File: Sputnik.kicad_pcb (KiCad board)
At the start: 4 copper layers, 130 x 65 mm, 177 parts, among them IC1 EP4CE10F17, J1 Pinheader_2x5_TH_WALL, P1 USB_A, U1 SN74LVC2T45, U10 SN74LVC8T245, U11 SN74LVC8T245, U12 SN74LVC8T245, U13 SN74LVC8T245, U14 SN74LVC8T245, U15 SN74LVC8T245, U16 SN74LVC2T45, U17 SN74LVC2T45, U18 SN74LVC2T45, U19 SN74LVC1G07DCK, U2 SN74LVC2T45, U20 SN74LVC2T45, U21 EPCS4, U22 W9751G6KB, U23 FT313HL-LQFP64-0.5, U24 TLV62569P, U25 TPS2024D, U3 SN74LVC1G07DCK, U4 SN74LVC2T45, U5 DM9000B, U6 93LC46, U7 74LVC2G07, U8 Pulse-J00-0045NL, U9 SN74LVC8T245, X2 Zorro_Connector, Y1 25MHz, Y2 12MHz

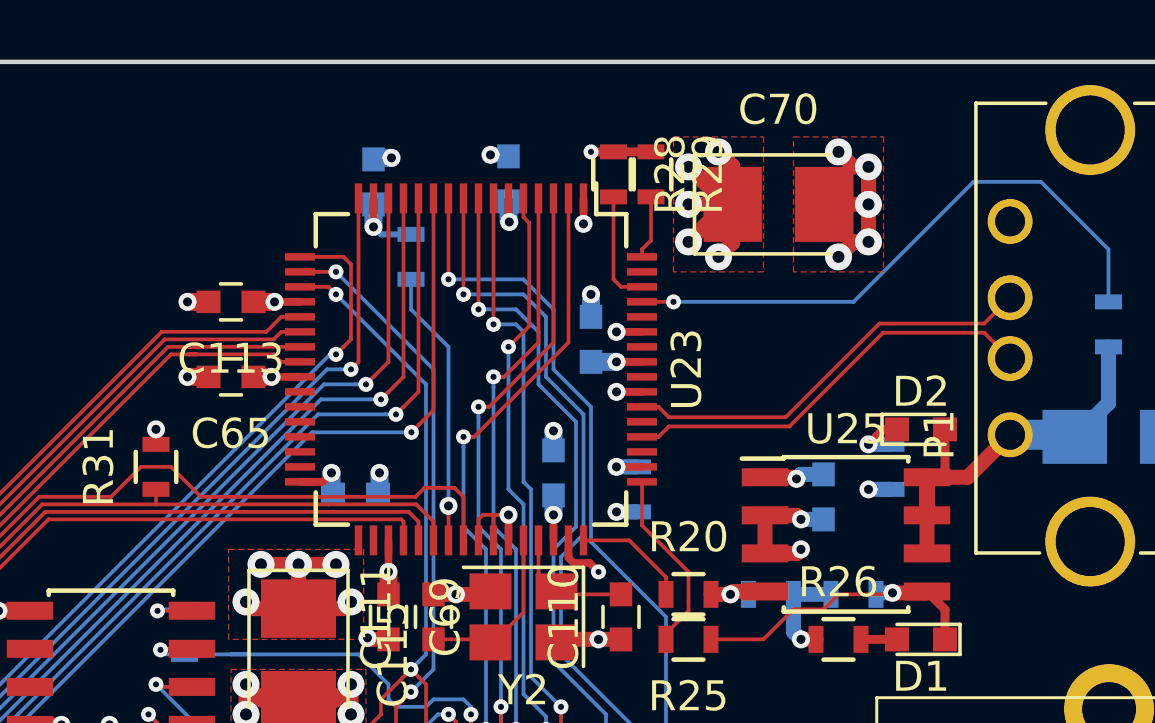
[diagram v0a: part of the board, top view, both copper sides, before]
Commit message: FT313 unused A0..A7 lines tied to GND
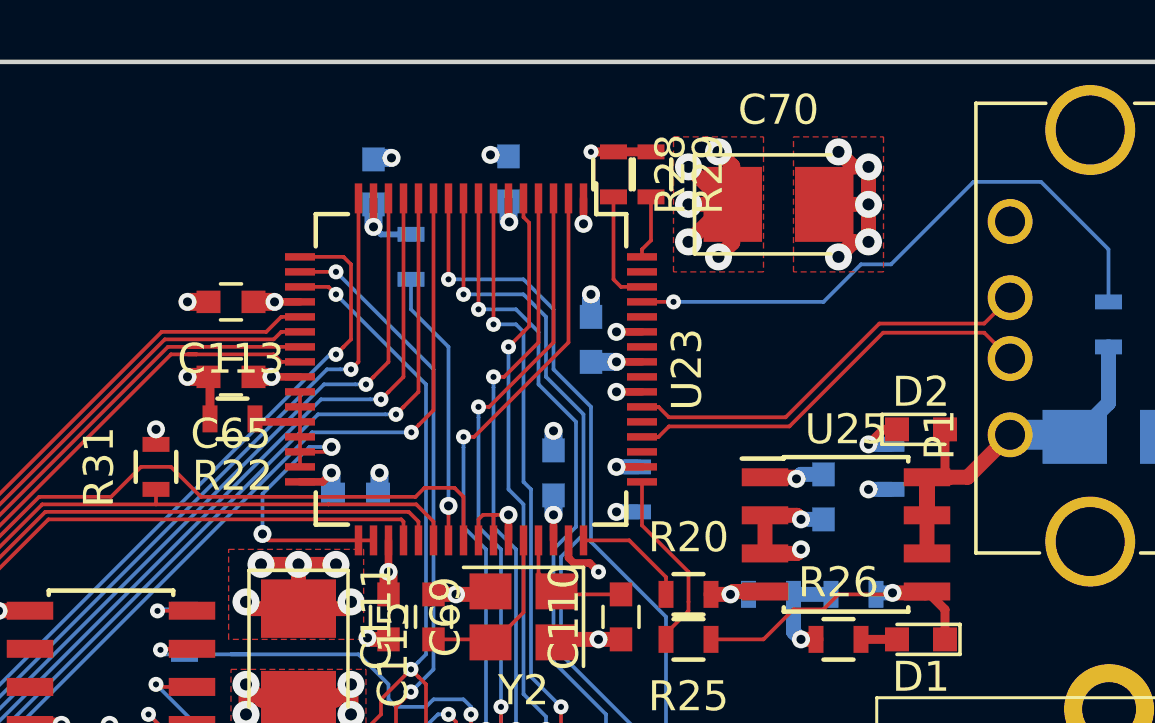
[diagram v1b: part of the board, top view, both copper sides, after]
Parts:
- added R22: 10K, Resistors_SMD:R_0603, F.Cu at (210.3, 26.9)
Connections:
- U23 pad 26: /usb/A0 -> Net-(R22-Pad1)
- U23 pad 27: /usb/A1 -> Net-(R22-Pad1)
- U23 pad 28: /usb/A2 -> Net-(R22-Pad1)
- U23 pad 29: /usb/A3 -> Net-(R22-Pad1)
- U23 pad 30: /usb/A4 -> Net-(R22-Pad1)
- U23 pad 31: /usb/A5 -> Net-(R22-Pad1)
- U23 pad 33: /usb/A6 -> Net-(R22-Pad1)
- U23 pad 34: /usb/A7 -> Net-(R22-Pad1)
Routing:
- net Net-(R22-Pad1): track 0.00 -> 13.2 mm, vias 0 -> 2
- net GND: track 279.6 -> 281.0 mm

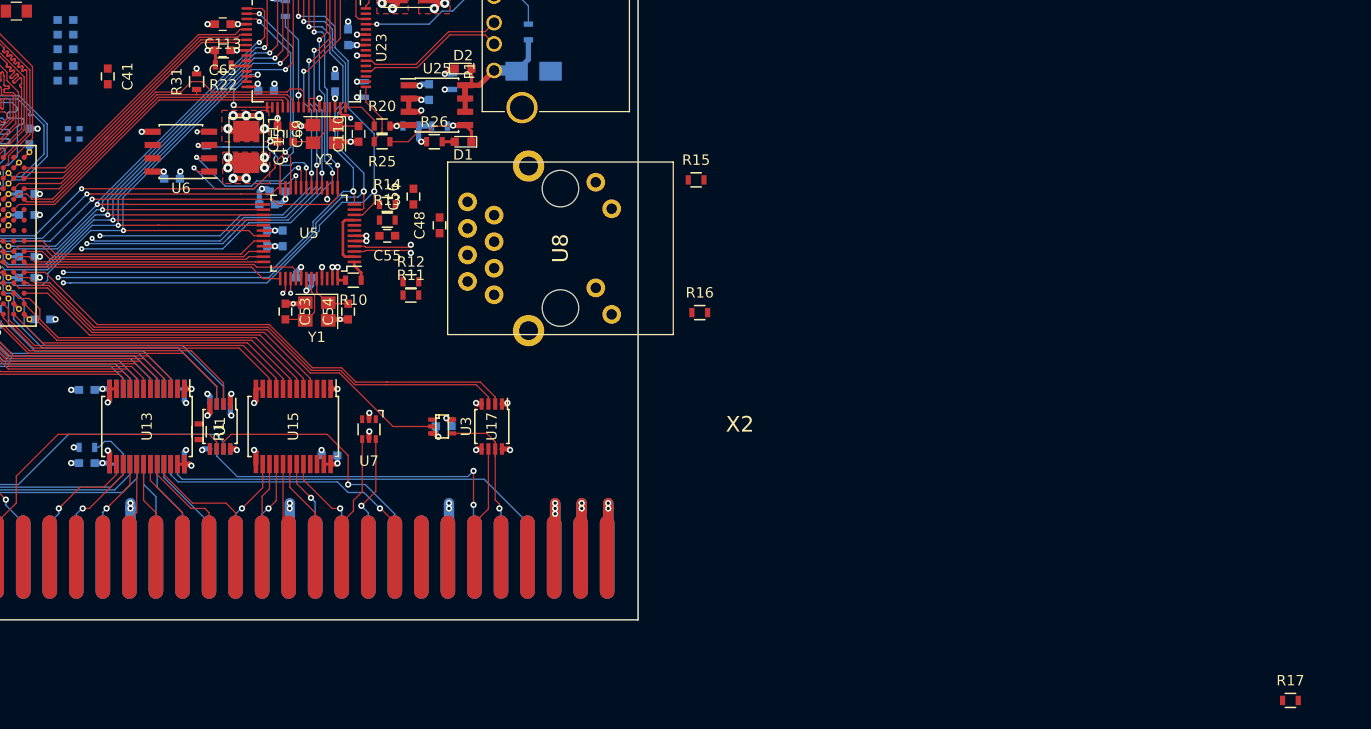
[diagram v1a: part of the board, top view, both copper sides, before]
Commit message: Shield copper pour for RJ45
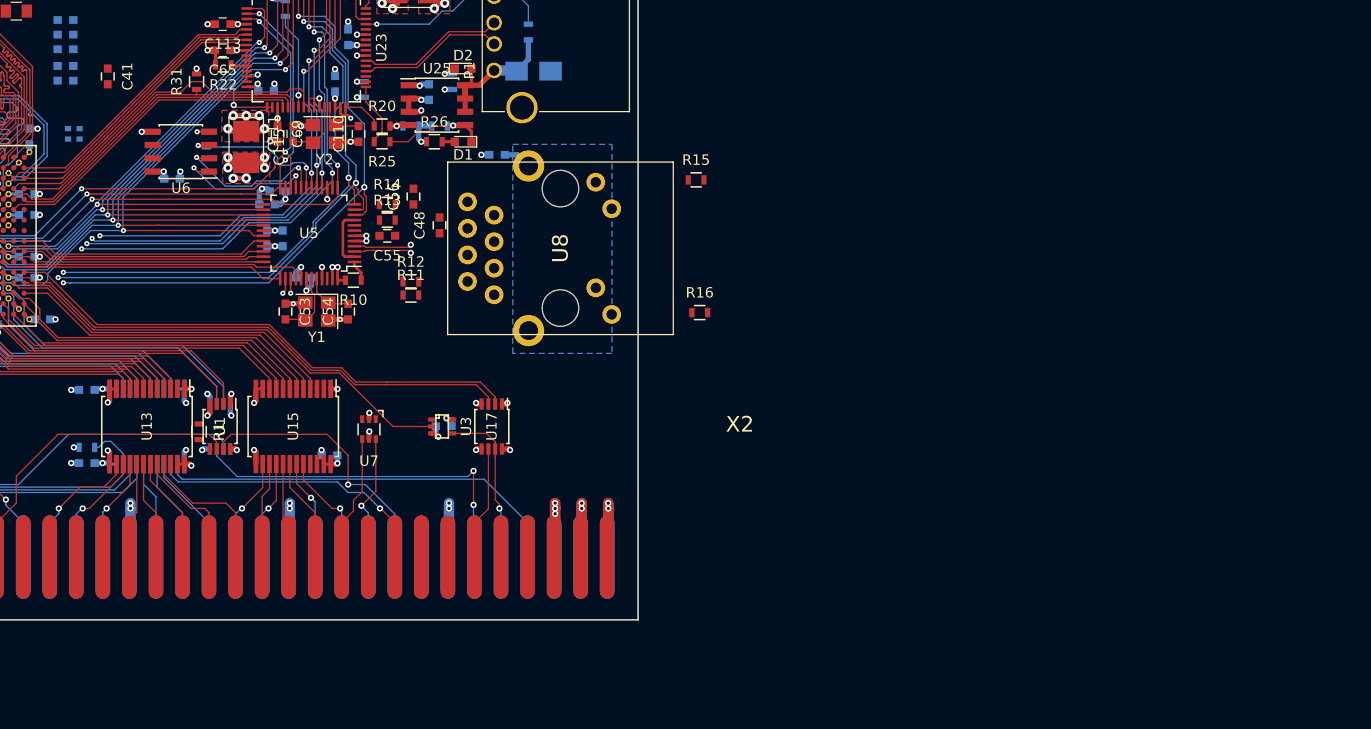
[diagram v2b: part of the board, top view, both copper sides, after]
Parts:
- removed R17: 000, Resistors_SMD:R_0603
- added C116: 0,1, Capacitors_SMD:C_0603, B.Cu at (236.5, 35.5)
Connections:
- C55 pad 2: GNDA -> GND
- C56 pad 2: GNDA -> GND
- IC1 pad E12: GNDA -> GND
- IC1 pad M5: GNDA -> GND
- R10 pad 2: GNDA -> GND
- U5 pad 47: GNDA -> GND
- U5 pad 48: GNDA -> GND
- U5 pad 5: GNDA -> GND
- U5 pad 6: GNDA -> GND
- U8 pad 8: GNDA -> GND
- U8 pad S: GNDA -> GNDPWR
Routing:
- net GND: track 281.0 -> 287.8 mm, vias 147 -> 152
- net GNDA: track 6.02 -> 0.00 mm, vias 4 -> 0
- net GNDPWR: track 0.00 -> 2.72 mm
- net ETHSD7: track 71.4 -> 69.7 mm
- net ETHSD6: track 70.1 -> 69.1 mm
- net ETHSD5: track 66.8 -> 67.4 mm
- added copper zone on B.Cu, net GNDPWR
- removed copper zone on In1.Cu, net GNDA

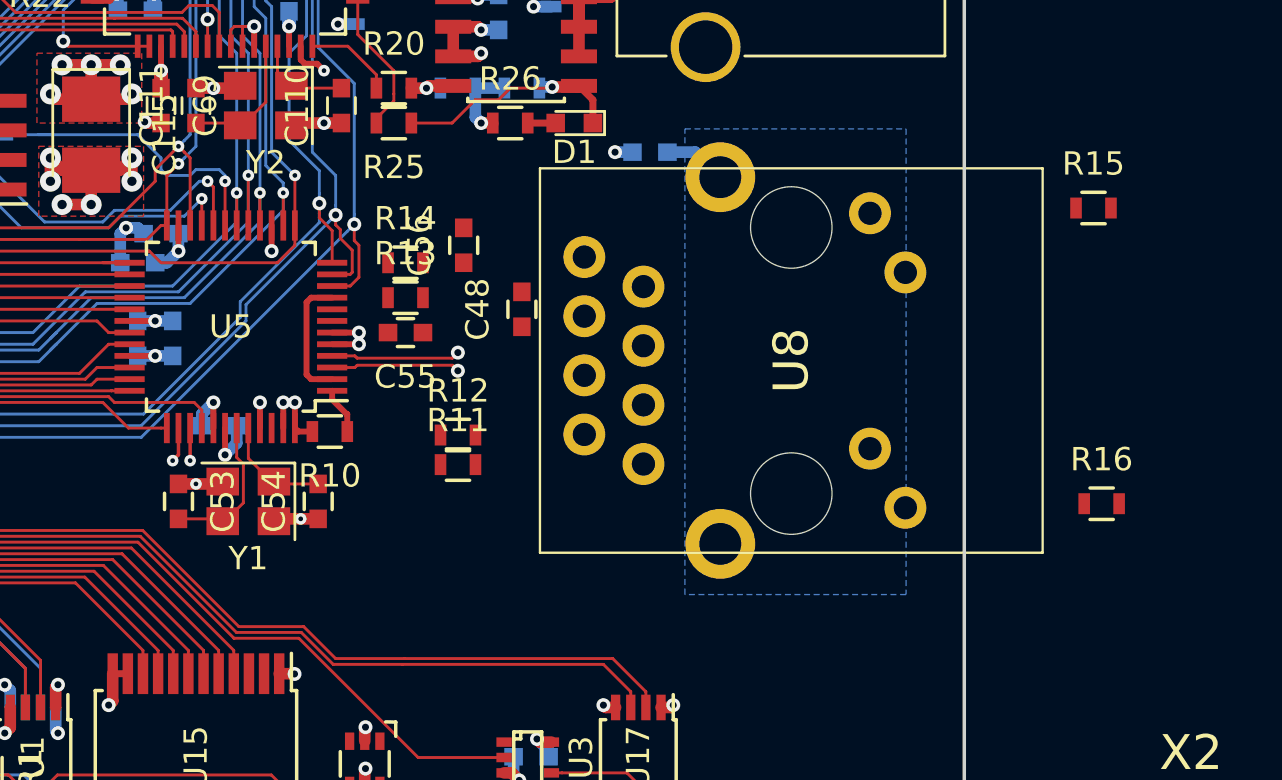
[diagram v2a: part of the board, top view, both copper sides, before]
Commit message: TX/RX pairs routed
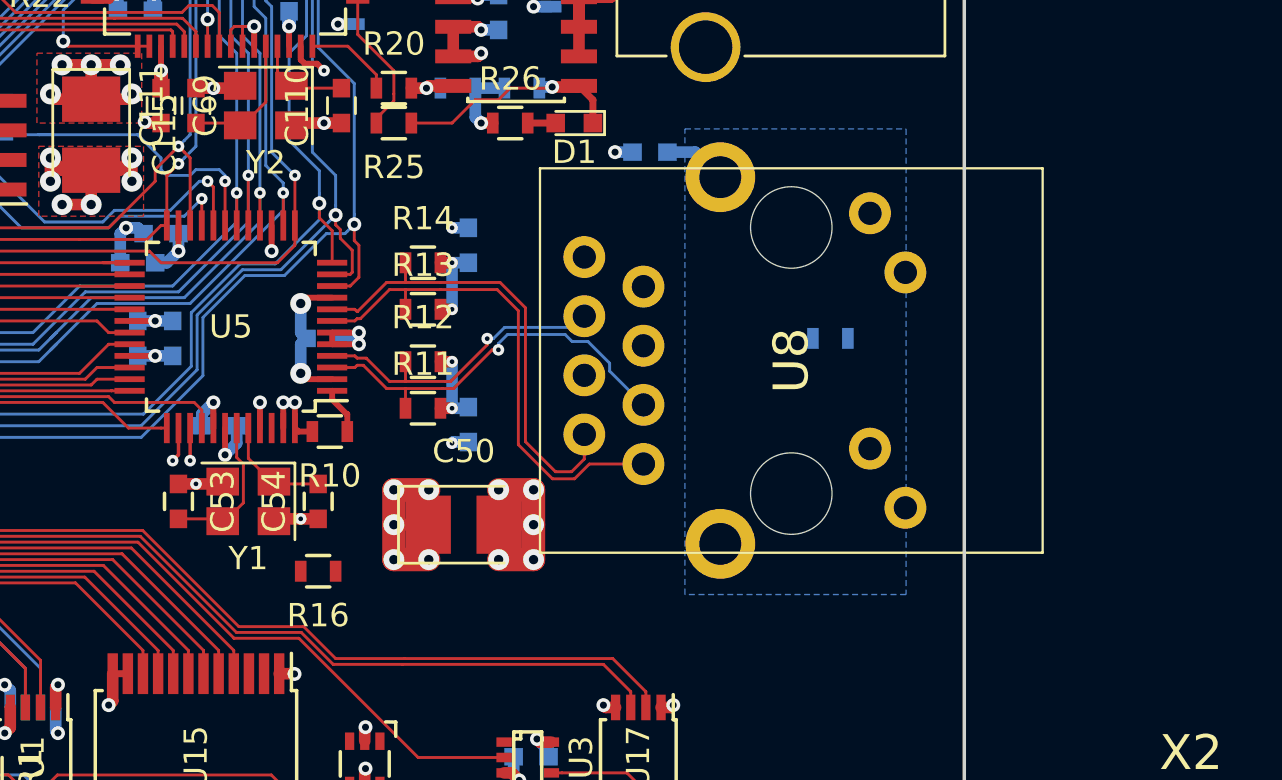
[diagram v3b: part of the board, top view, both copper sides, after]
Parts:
- added C50: 220x16, Capacitors_Tantalum_SMD:CP_Tantalum_Case-B_EIA-3528-21_Reflow, F.Cu at (228.5, 51.5)
- C48, C55, C56, R15: moved to B.Cu
- moved R16 33.8 mm to (222.2, 53.5), turned to 180 degrees
- moved R15 12.6 mm to (244.2, 43.5)
- moved C48 8.59 mm to (222.5, 43.5), turned to 0 degrees
- moved C55 4.78 mm to (228.7, 47.2), turned to 270 degrees
- moved R12 3.49 mm to (226.8, 44.5)
- moved R11 2.85 mm to (226.8, 46.5)
- moved R13 0.90 mm to (226.8, 42.2)
- moved R14 0.75 mm to (226.8, 40.2)
- moved C56 0.20 mm to (228.7, 39.5)
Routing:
- net /ethernet/TX_P: track 0.00 -> 21.8 mm
- net /ethernet/TX_N: track 0.00 -> 20.8 mm
- net /ethernet/RX_P: track 5.54 -> 17.2 mm
- net GND: track 287.8 -> 298.4 mm, vias 152 -> 159
- net /ethernet/RX_N: track 5.54 -> 14.1 mm
- net AVDD18: track 5.47 -> 13.6 mm, vias 0 -> 7
- net Net-(C55-Pad1): track 0.00 -> 3.72 mm, vias 0 -> 2
- net Net-(C56-Pad1): track 0.00 -> 3.70 mm, vias 0 -> 2
- net ETHSD7: track 69.7 -> 71.2 mm
- net ETHSD6: track 69.1 -> 70.0 mm
- net ETHSD5: track 67.4 -> 68.2 mm
- added copper zone on In2.Cu, net AVDD18

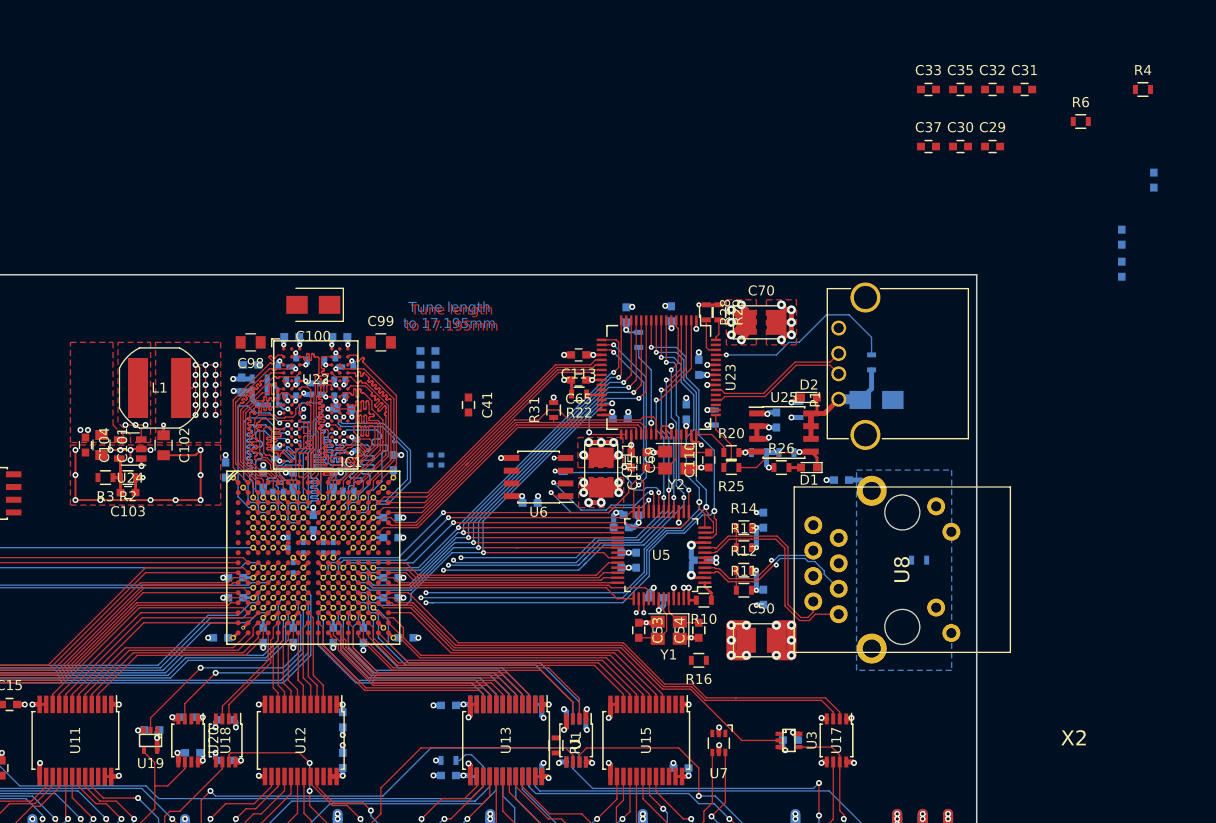
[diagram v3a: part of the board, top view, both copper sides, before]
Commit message: +5V routing
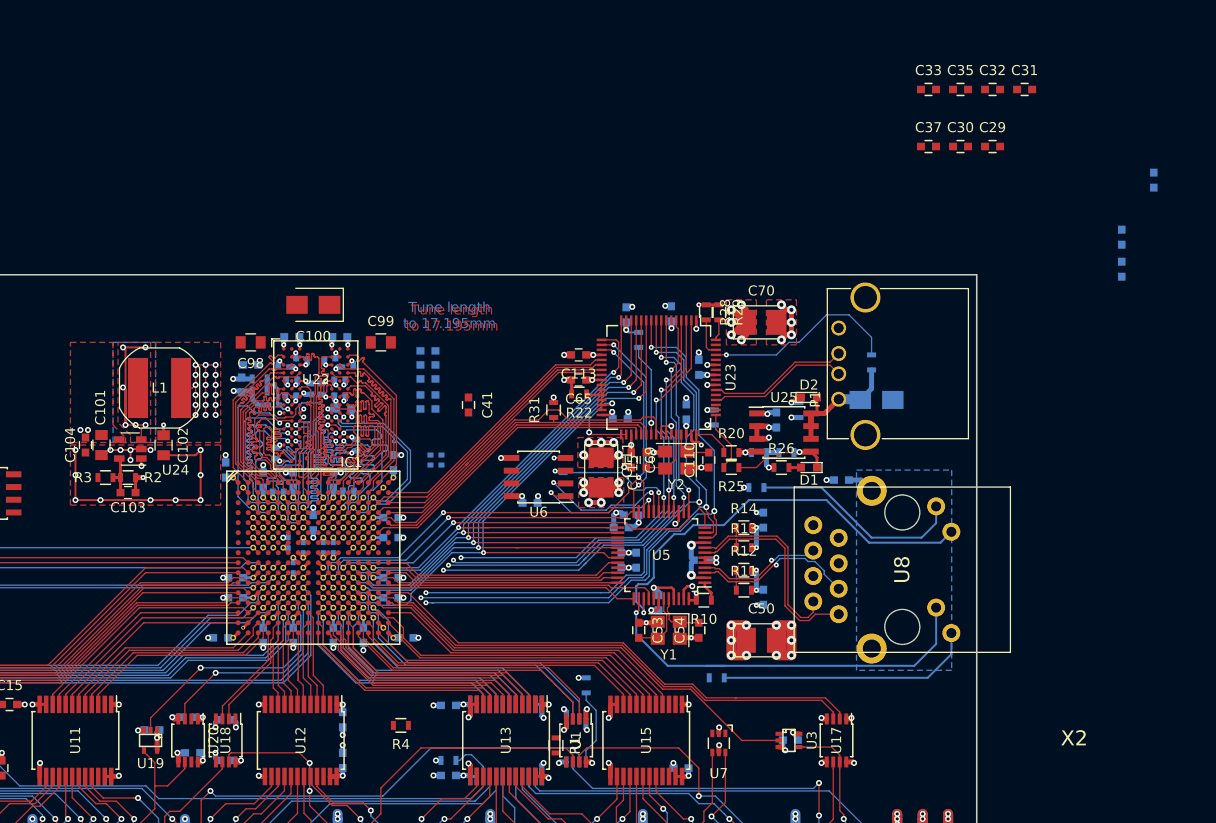
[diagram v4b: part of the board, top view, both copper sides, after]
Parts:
- R16, R6: moved to B.Cu
- moved R4 97.6 mm to (192.5, 60.0), turned to 180 degrees
- moved R6 74.9 mm to (211.0, 56.0), turned to 270 degrees
- moved R15 17.8 mm to (228.0, 36.2)
- moved R16 2.50 mm to (224.0, 55.2)
- moved C45 0.56 mm to (218.2, 47.8), turned to 90 degrees
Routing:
- net /ethernet/LED1: track 1.40 -> 43.0 mm
- net /ethernet/LED2: track 1.50 -> 41.3 mm
- net Net-(R16-Pad1): track 0.00 -> 25.8 mm
- net Net-(R15-Pad2): track 0.00 -> 21.5 mm
- net /Power/SW1V8: track 3.63 -> 17.6 mm, vias 3 -> 6
- net Net-(R6-Pad2): track 0.00 -> 7.74 mm
- net +5VDC: track 119.7 -> 124.1 mm
- net GND: track 298.4 -> 300.7 mm, vias 159 -> 158
- net +3V3: track 74.2 -> 75.4 mm, vias 32 -> 34
- net Net-(R20-Pad2): track 1.84 -> 2.44 mm
- net Net-(C54-Pad2): track 4.76 -> 5.29 mm
- added copper zone on B.Cu, net /Power/SW1V8

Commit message: More PCB work
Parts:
- moved R16 11.2 mm to (214.2, 49.8), turned to 90 degrees
- moved C56 4.23 mm to (226.0, 42.8), turned to 180 degrees
- moved C55 4.00 mm to (226.0, 44.2), turned to 180 degrees
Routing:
- net Net-(R16-Pad1): track 25.8 -> 37.3 mm
- net +5VDC: track 124.1 -> 117.7 mm, vias 21 -> 25
- net GND: track 300.7 -> 305.0 mm
- net /ethernet/LED1: track 43.0 -> 46.6 mm
- net ETHSD3: track 62.1 -> 65.2 mm
- net Net-(R15-Pad2): track 21.5 -> 19.4 mm
- net ETHSD7: track 71.2 -> 73.2 mm
- net /ethernet/LED2: track 41.3 -> 39.9 mm
- net Net-(C56-Pad1): track 3.70 -> 4.46 mm
- net +3V3: track 75.4 -> 76.1 mm, vias 34 -> 35
- net Net-(IC1-PadF6): track 0.00 -> 0.71 mm
- net Net-(IC1-PadF11): track 0.00 -> 0.71 mm
- net Net-(IC1-PadF5): track 0.00 -> 0.71 mm
- net /fpga/VCCA2: track 0.00 -> 0.71 mm
- net Net-(IC1-PadF9): track 0.00 -> 0.71 mm
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- added copper zone on B.Cu, net +5VDC
- added copper zone on F.Cu, net /usb/VBUS
